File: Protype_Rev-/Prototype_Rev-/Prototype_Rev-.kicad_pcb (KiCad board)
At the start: 2 copper layers, 59.9 x 66.3 mm, 109 parts, among them J1 USB_B_Micro, J2 Interface Hub, J3 Conn_01x02, Q1 SS8050-G, Q2 SS8050-G, Q3 2N7002ET7G, Q4 BSS83P, SW1 EN, SW2 BOOT, U1 MAX30101EFD+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

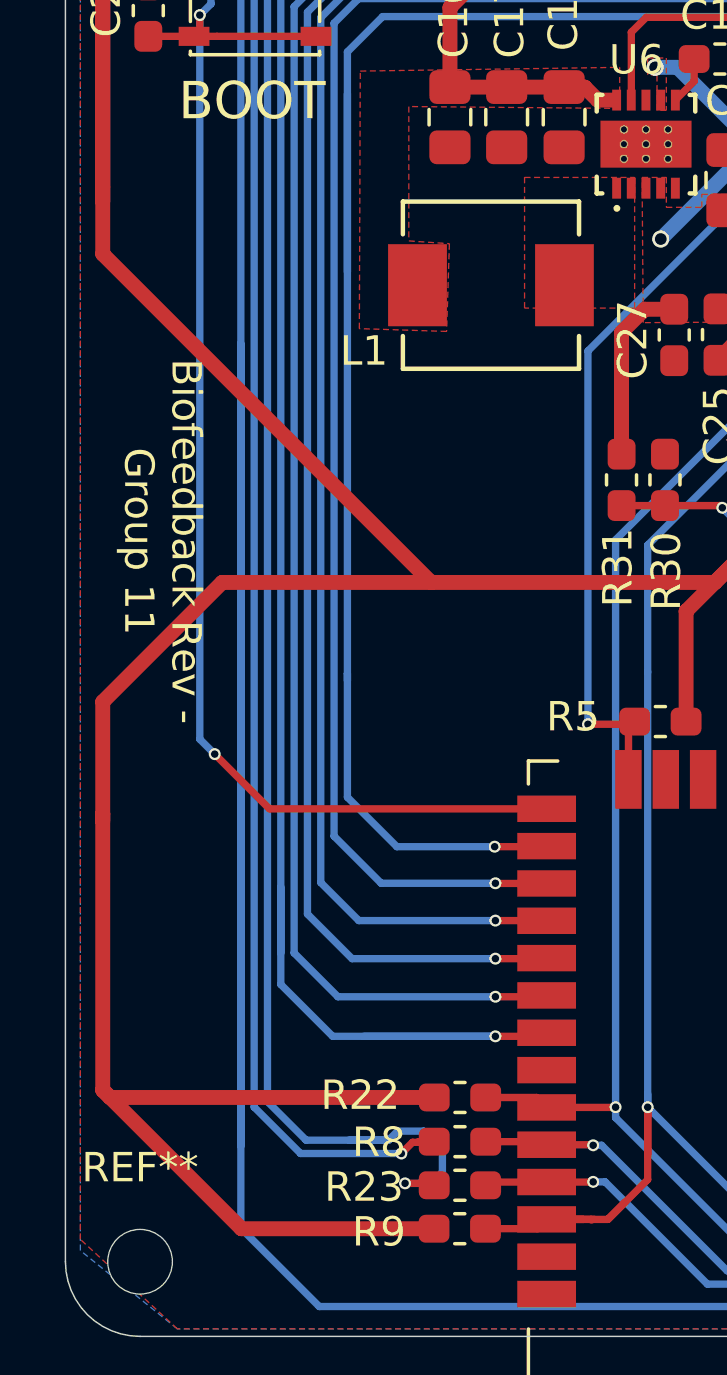
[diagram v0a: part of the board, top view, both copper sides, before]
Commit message: Prototype rev - completed. Connectors added and STEP file generated. Phone app progress
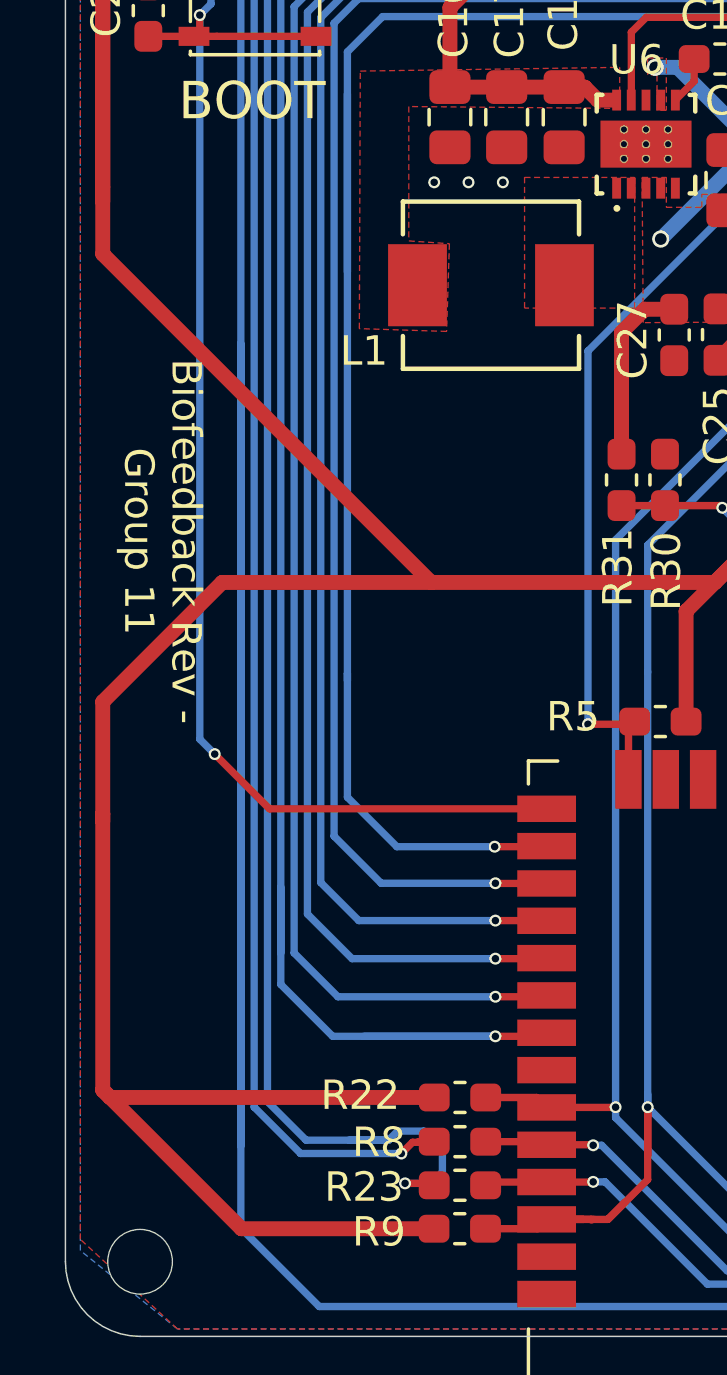
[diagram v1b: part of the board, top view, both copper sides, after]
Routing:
- net GND: vias 52 -> 55
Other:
- board text added: "+"
- board text added: "-"
- board text added: "BATT"
- board text added: "Conn Config"
- board text added: "Connector"
- board text added: "GSR"
- board text added: "HIGH"
- board text added: "LOW (GND)"
- board text added: "MIDDLE"
- board text added: "RX"
- board text added: "SERIAL"
- board text added: "See the connector above for the proper polarities"
- board text added: "TEMP"
- board text added: "TX"
